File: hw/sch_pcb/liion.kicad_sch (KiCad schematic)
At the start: 64 parts, among them Q3 BC807-25, Q4 BC817-25, SW1 SW_Push, U1 BQ34Z100, U2 SN74HC164D, U8 BQ25628E

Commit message: WIP, routing
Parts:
- SW1: value SW_Push -> SKRTLAE010
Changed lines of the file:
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@@
       (effects (font (size 1.27 1.27)))
     )
-    (property "Value" "SW_Push" (at 43.18 80.01 0)
+    (property "Value" "SKRTLAE010" (at 43.18 80.01 0)
       (effects (font (size 1.27 1.27)))
     )

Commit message: WIP
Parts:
- D1, D2, D3, D4, D5: UST_ID 5c70984412875079b91f8897 -> (none)
- L1: UST_ID 650b5977462c6d9e72054656 -> (none)
- R4: UST_ID 5c70984712875079b91f8ac5 -> (none)
- SW1: symbol Switch:SW_Push -> MLAB_SW:SW_Push_shield
- U1: UST_ID 5c70984612875079b91f89c3 -> (none)
- renumbered R24 to R23, R27 to R26, R28 to R27, TH1 to TH2
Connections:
- net GND: now also SW1.GND (SHIELD)

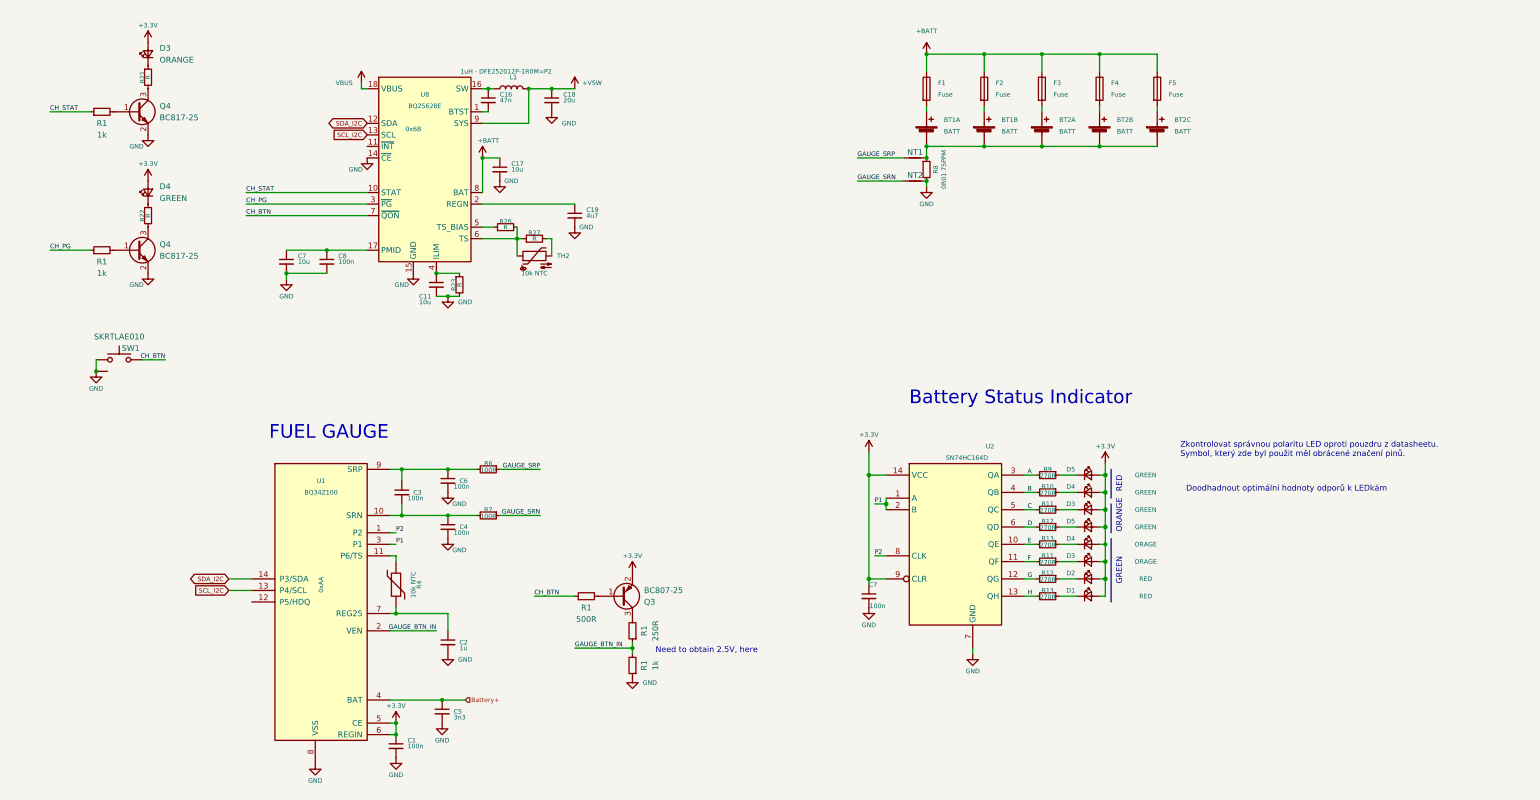
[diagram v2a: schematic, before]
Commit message: wip, split power adapter to BATDATSOCKET01
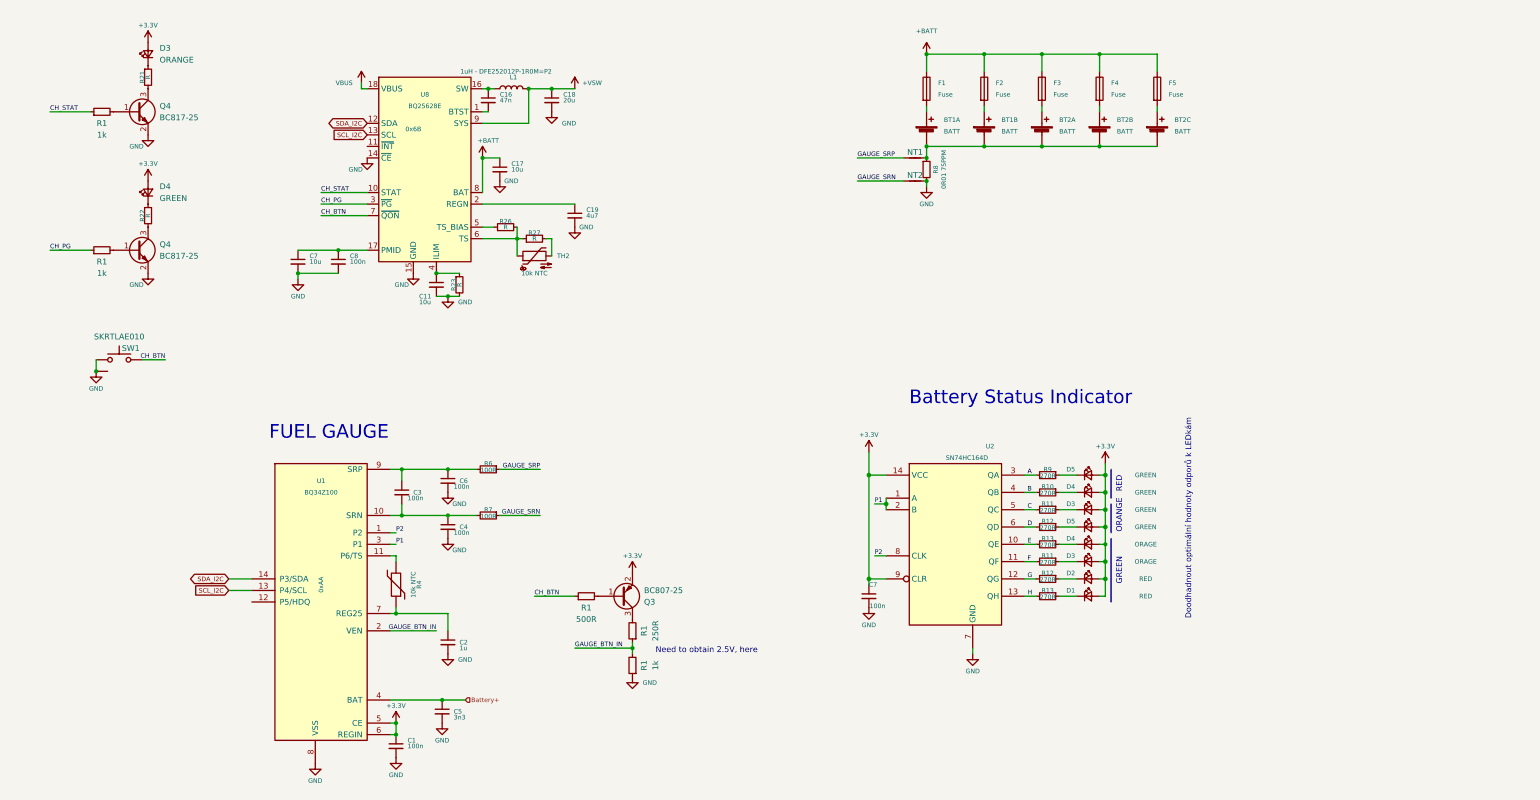
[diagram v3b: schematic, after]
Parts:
- BT1: UST_ID (none) -> 5c70984412875079b91f87e9
- BT2: UST_ID (none) -> 63567f66c8e7b5bbef872ce1
- F1, F2, F3, F4, F5: UST_ID (none) -> 5c70984512875079b91f88d8
- R4, TH2: UST_ID (none) -> 5c70984712875079b91f8ac5
- R6, R7: UST_ID (none) -> 5c70984512875079b91f8977
- R8: UST_ID (none) -> 5c70984712875079b91f8abf
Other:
- note removed: "Zkontrolovat správnou polaritu LED oproti pouzdru z datasheetu. Symbol, který zde byl použit měl obrácené značení pinů."
- company: (none) -> MLAB.cz
- title: (none) -> BATDATUNTI01
- moved on the sheet: C7, C8

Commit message: WIP, add ust ID for existing parts
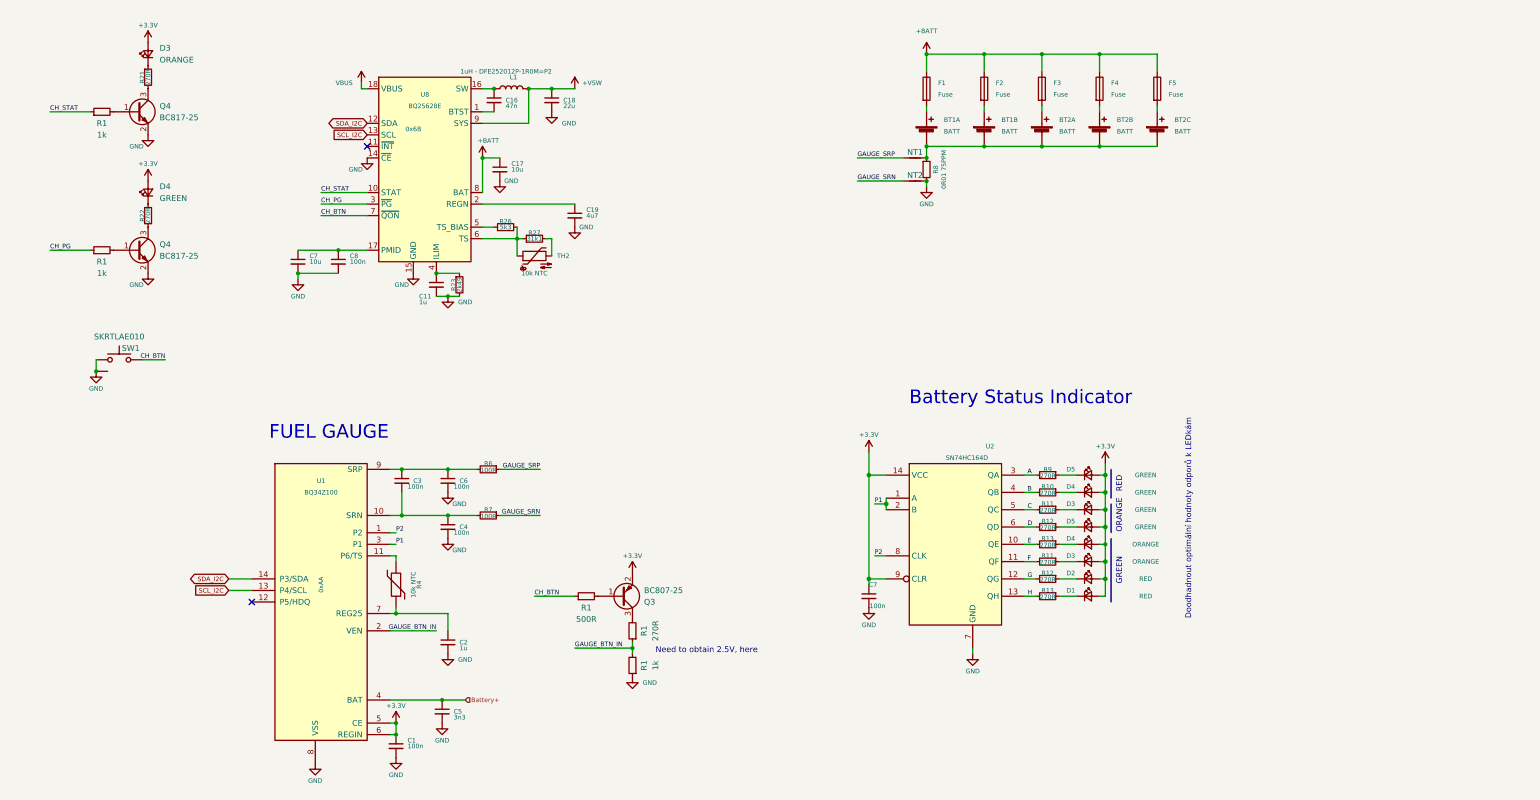
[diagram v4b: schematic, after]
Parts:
- C1, C3, C4, C6, C7, C8: UST_ID (none) -> 5c70984712875079b91f8b4c
- C11: value 10u -> 1u; UST_ID (none) -> 5c70984712875079b91f8b50
- C17, C7: UST_ID (none) -> 5c70984712875079b91f8b53
- C18: value 20u -> 22u; UST_ID (none) -> 650b58f1462c6d9e7205463b
- C19: UST_ID (none) -> 5c70984712875079b91f8b52
- C2: UST_ID (none) -> 5c70984712875079b91f8b50
- C5: UST_ID (none) -> 5c70984712875079b91f8b47
- D3, D4: value ORAGE -> ORANGE
- L1: UST_ID (none) -> 650b5977462c6d9e72054656
- NT1, NT2: UST_ID (none) -> x
- Q3: value BC807-25 -> BC807-25; UST_ID (none) -> 5c70984712875079b91f8aeb
- Q4: UST_ID (none) -> 5c70984712875079b91f8aea
- R1: UST_ID (none) -> 5c70984512875079b91f898c
- R1: value 250R -> 270R
- R21, R22: value R -> 270R
- R23: value R -> 2k49
- R26: value R -> 5k3
- R27: value R -> 31k1
- U1: UST_ID (none) -> 5c70984612875079b91f89c3
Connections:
- no-connect marks 0 -> 2
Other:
- moved on the sheet: C16, C3

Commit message: WIP, schematic improvements, bigger page, reststructualized
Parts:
- renumbered C7 to C20, C8 to C21, C11 to C24, C16 to C29, C17 to C30, C18 to C31, C19 to C32, D3 to D6, D4 to D7, Q3 to Q5, R21 to R45, R22 to R46, R23 to R47, R26 to R50, R27 to R51, SW1 to SW4, U8 to U13
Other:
- moved on the sheet: BT1A, BT1B, BT2A, BT2B, BT2C, C1, C31, C5, D6, F1, F2, F3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

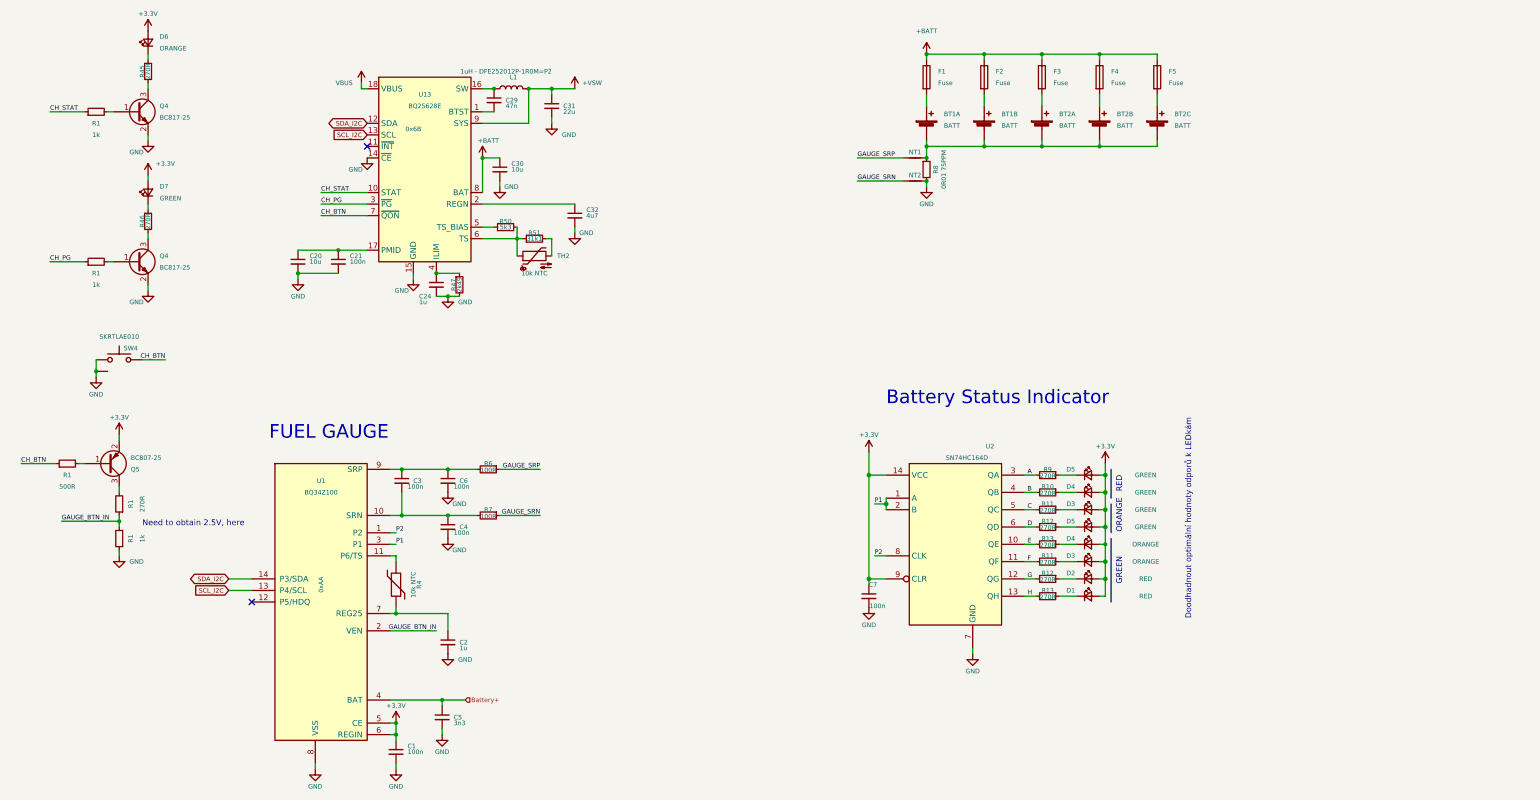
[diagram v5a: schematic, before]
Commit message: Updates in schematics, improved readability
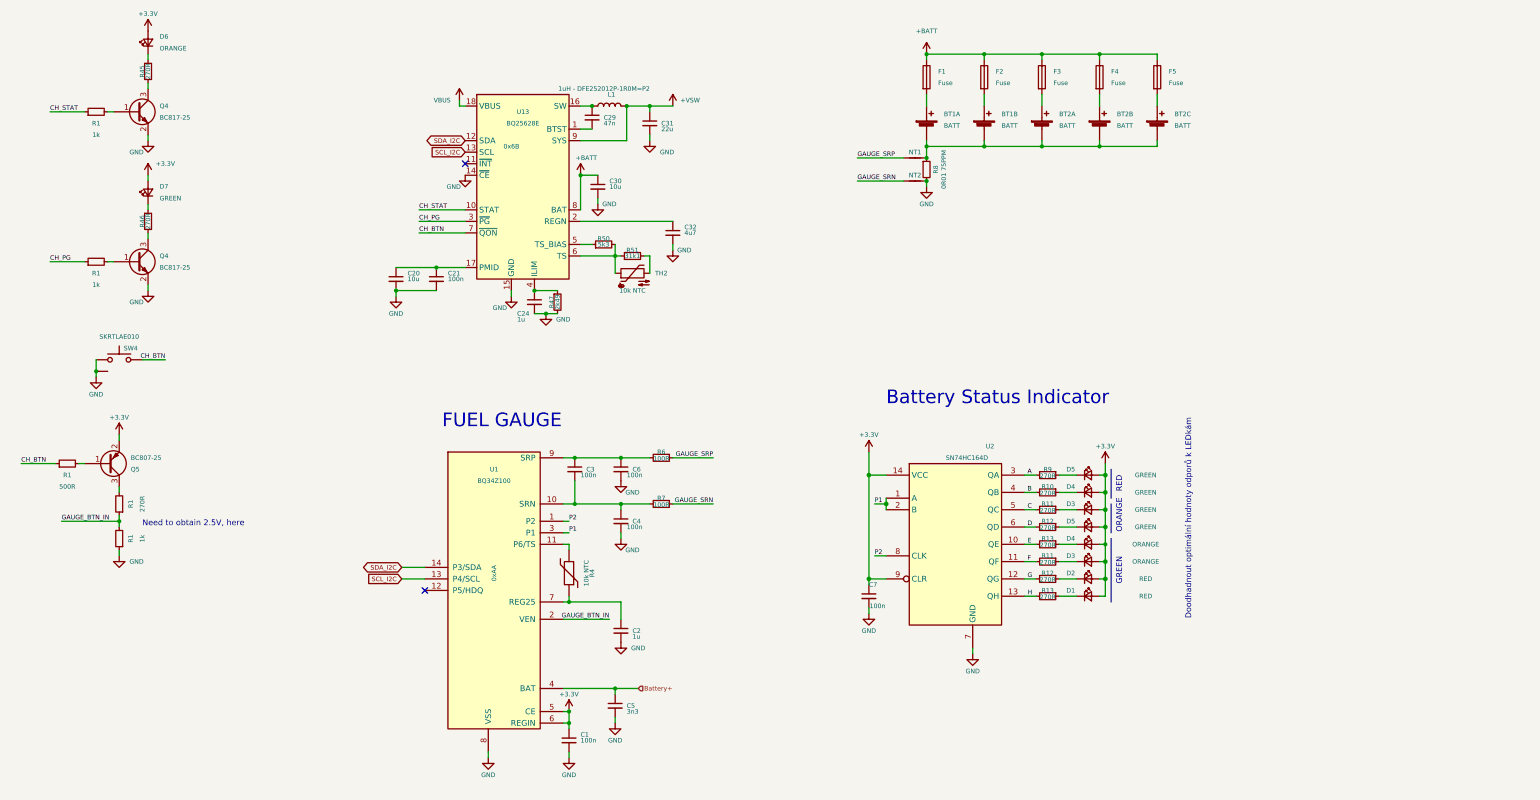
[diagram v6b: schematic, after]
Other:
- moved on the sheet: C1, C2, C20, C21, C24, C29, C3, C30, C31, C32, C4, C5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
